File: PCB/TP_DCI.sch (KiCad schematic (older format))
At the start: 70 parts, among them J8 Molex_KK254, J9 Molex_KK254, K1 G5V-1, K2 G5V-1, P1 Conn_Poncho2P_2x_20x2, Q1 BC817W, Q2 BC817W, U1 PS2805-4, U2 ACS725xLCTR-10AU, U4 ACS725xLCTR-10AU, U5 24AA1025, U6 DS3231

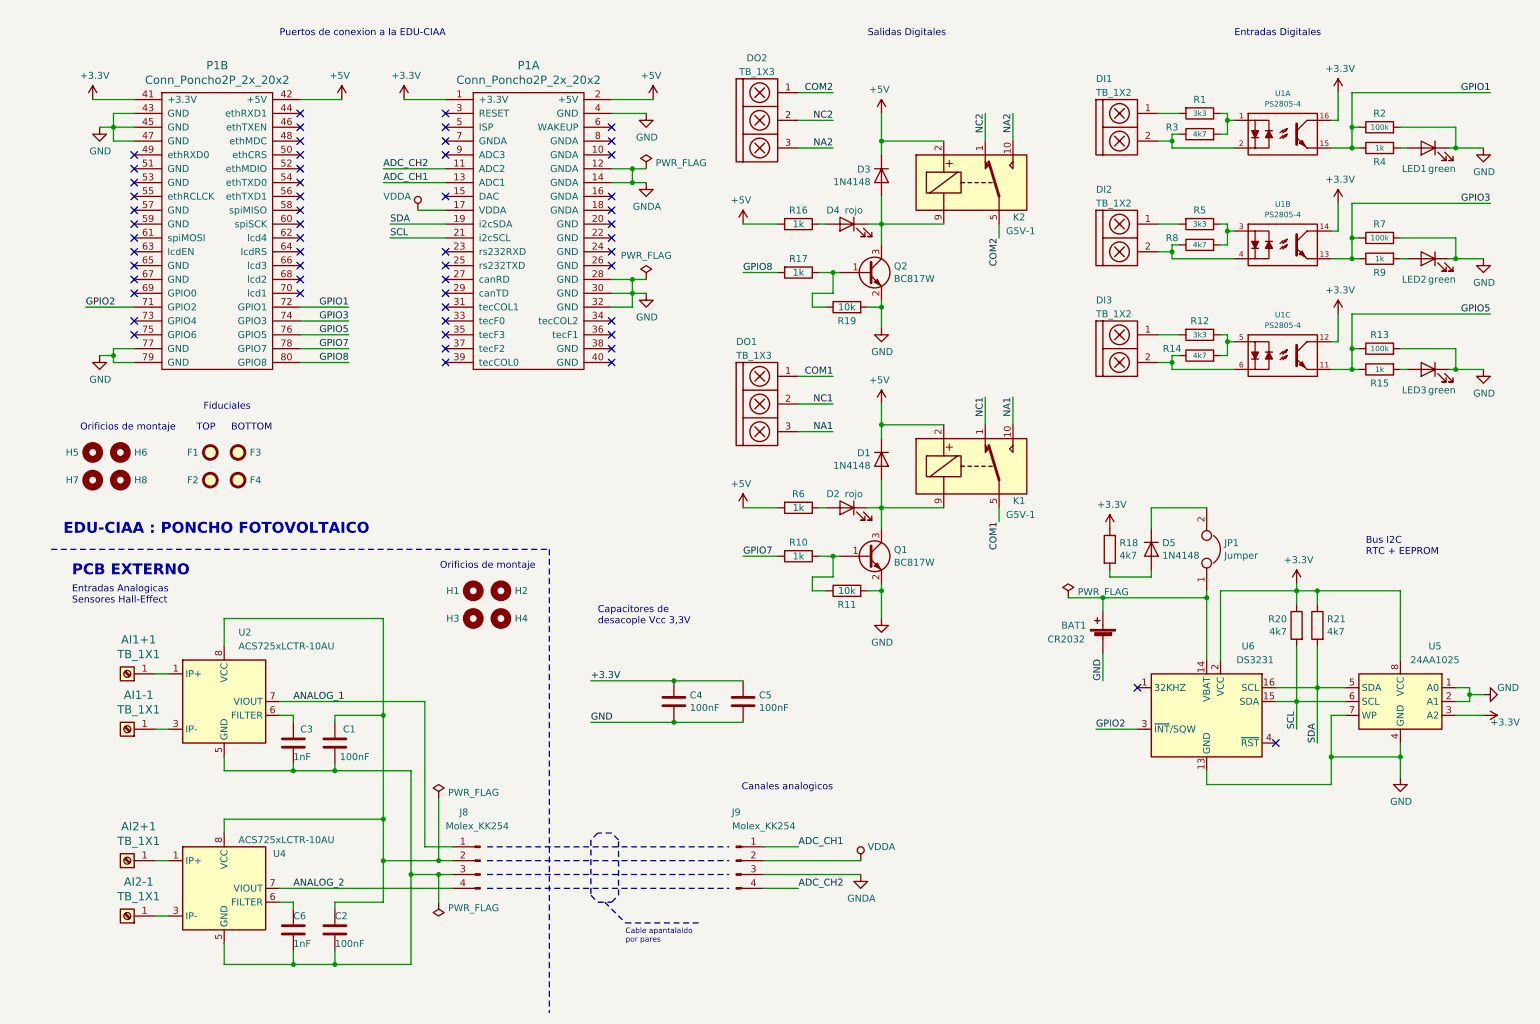
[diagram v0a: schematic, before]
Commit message: actualizaciones de esquematico segun correcciones del docente
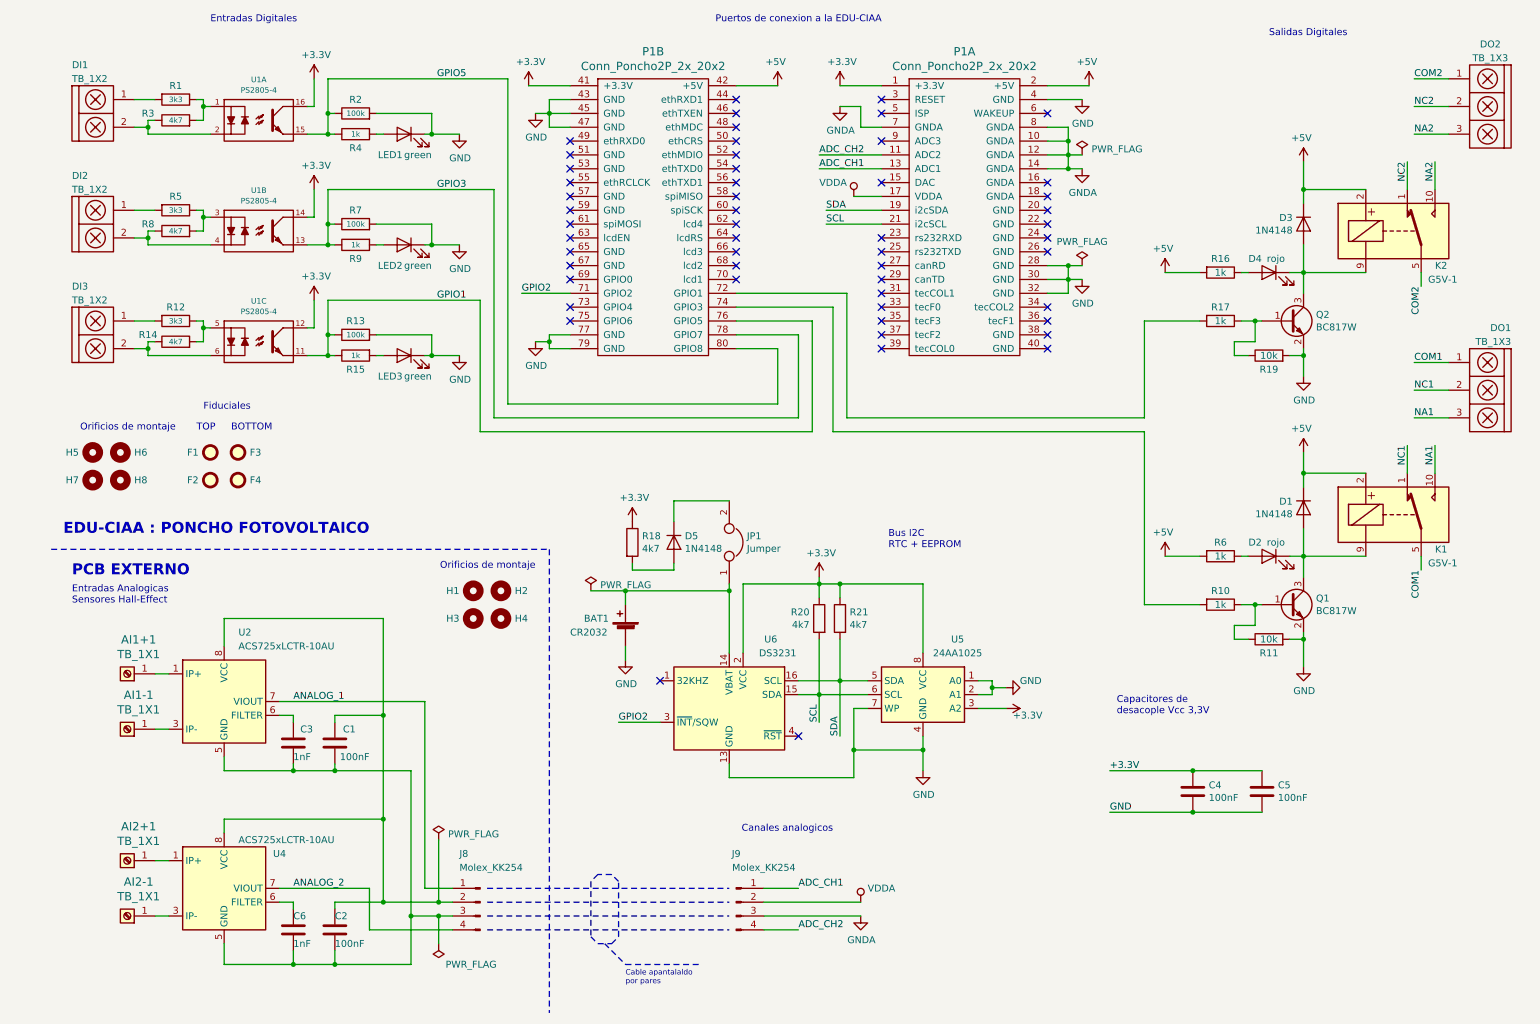
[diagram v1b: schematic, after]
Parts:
- F1, F2, F3, F4: footprint Fiducial:Fiducial_0.5mm_Mask1mm -> Fiducial:Fiducial_1mm_Mask2mm
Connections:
- net GNDA: now also P1.10 (GNDA), P1.7 (GNDA), P1.8 (GNDA)
- net GPIO1: now also P1.76 (GPIO5), R13.1, R15.1, U1.11; no longer P1.72 (GPIO1), R2.1, R4.1, U1.15
- net GPIO3: now also P1.78 (GPIO7); no longer P1.74 (GPIO3)
- net GPIO5: now also P1.80 (GPIO8), R2.1, R4.1, U1.15; no longer P1.76 (GPIO5), R13.1, R15.1, U1.11
- net GPIO7: no longer names the net of R10.2
- net GPIO7: now also P1.74 (GPIO3); no longer P1.78 (GPIO7)
- net GPIO8: no longer names the net of R17.2
- net GPIO8: now also P1.72 (GPIO1); no longer P1.80 (GPIO8)
- no-connect marks 56 -> 53
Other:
- moved on the sheet: BAT1, C4, C5, D1, D2, D3, D4, D5, DI1, DI2, DI3, DO1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

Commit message: avances en ruteo del PCB
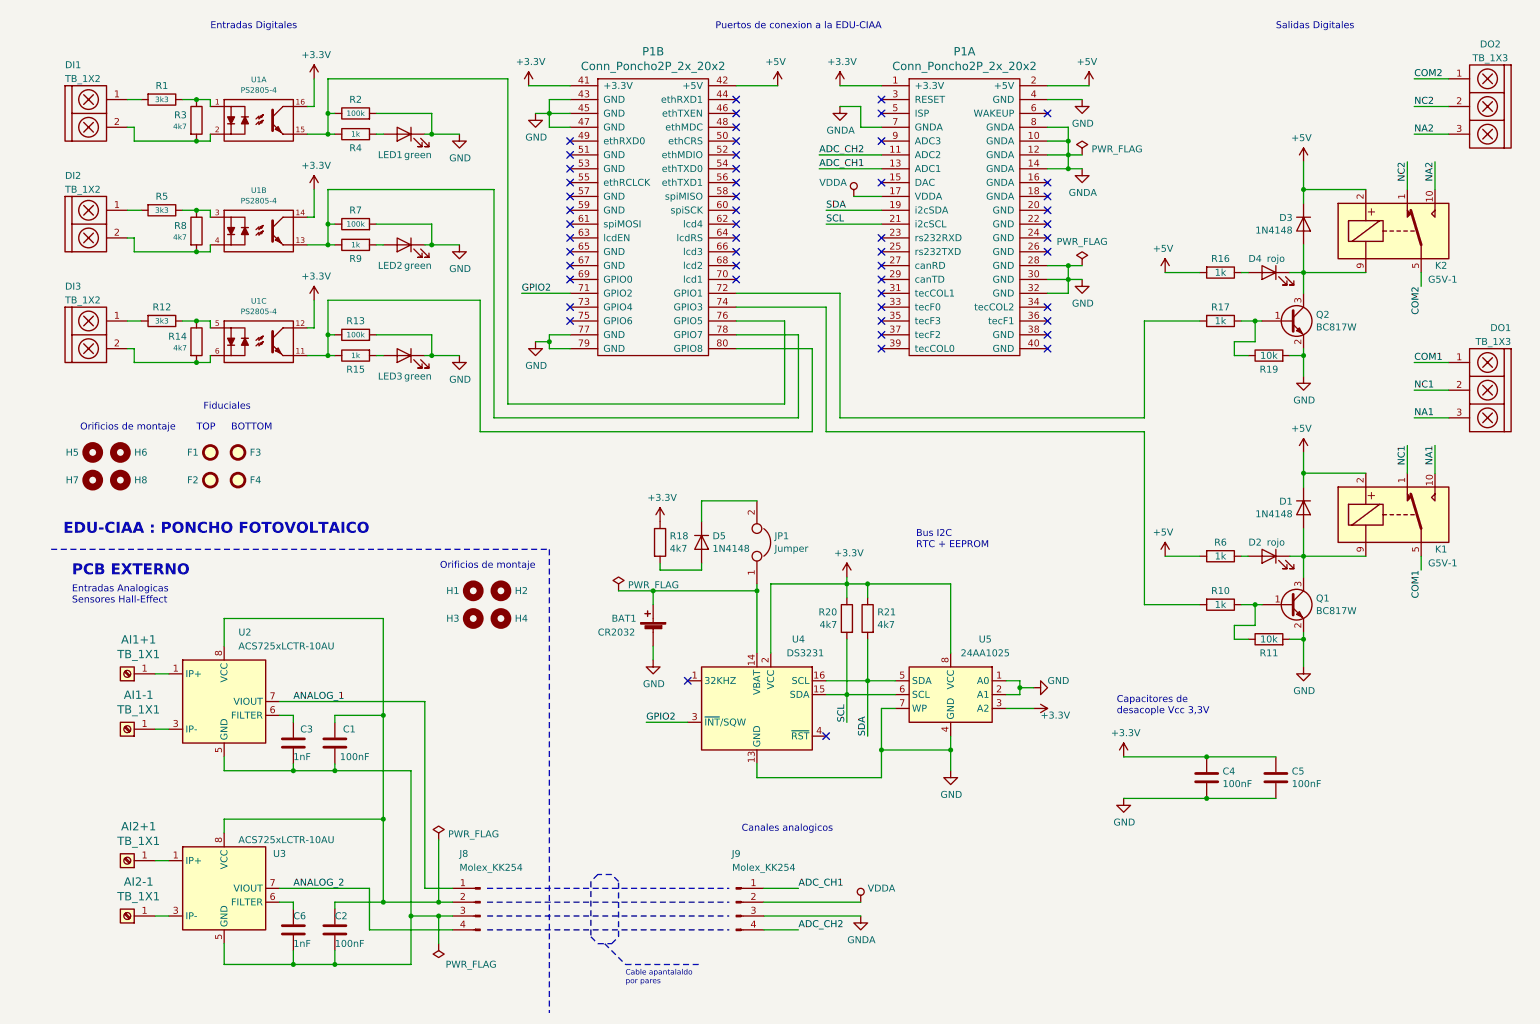
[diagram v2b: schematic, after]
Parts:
- U1: Codigo Digikey (none) -> PS2805-4A-ND
- U2: Codigo Digikey (none) -> 2100-201876-003-ND
- U3: renamed from U4; Codigo Digikey (none) -> 2100-201876-003-ND
- U4: renamed from U6; Codigo Digikey (none) -> DS3231S#T&RTR-ND
- U5: Codigo Digikey (none) -> 24AA1025-I/SN-ND
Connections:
- net +3.3V is gone; now on net +3V3: C4.1, C5.1
- net at R1.1, U1.1: now also R3.1; no longer R3.2
- net at DI1.2, U1.2: now also R3.2; no longer R3.1
- net at DI2.2, U1.4: now also R8.2; no longer R8.1
- net at DI3.2, U1.6: now also R14.2; no longer R14.1
- net at R5.1, U1.3: now also R8.1; no longer R8.2
- net at R12.1, U1.5: now also R14.1; no longer R14.2
- net GPIO1: no longer names the net of R13.1, R15.1, U1.11
- net GPIO1: now also P1.80 (GPIO8); no longer P1.76 (GPIO5)
- net GPIO3: no longer names the net of P1.78 (GPIO7), R7.1, R9.1, U1.13
- net GPIO5: no longer names the net of R2.1, R4.1, U1.15
- net GPIO5: now also P1.76 (GPIO5); no longer P1.80 (GPIO8)
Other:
- moved on the sheet: BAT1, C4, C5, D5, DI1, JP1, R1, R18, R20, R21, R3, U4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
